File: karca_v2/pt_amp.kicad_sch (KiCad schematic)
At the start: 12 parts, among them J6 Screw_Terminal_01x10, U10 TLV9304xD, U12 NUP4202, U34 MCP3204, U9 TLV9304xD

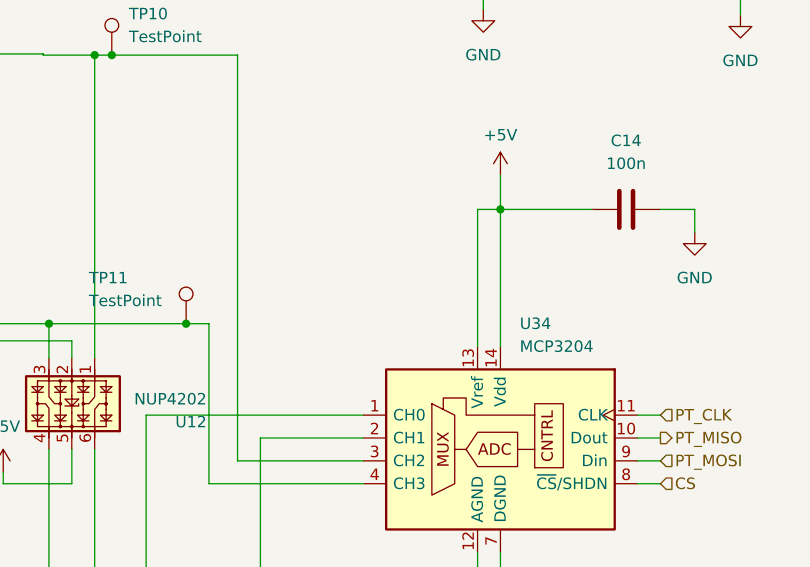
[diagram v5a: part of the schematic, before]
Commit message: finished schematic for v2.1
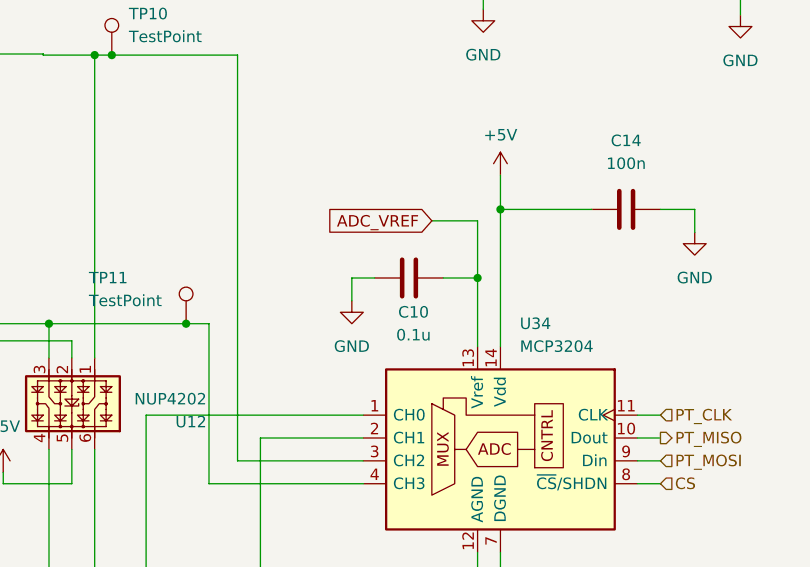
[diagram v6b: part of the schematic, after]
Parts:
- added C10: 0.1u, Capacitor_SMD:C_1206_3216Metric, symbol Device:C
- U34: footprint (none) -> Package_SO:SOIC-14_3.9x8.7mm_P1.27mm
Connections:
- net +5V: no longer U34.13 (Vref)
- net GND: now also C10.1
- new net ADC_VREF: C10.2, U34.13 (Vref)
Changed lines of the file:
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@@
+	)
+	(junction
+		(at 209.55 86.36)
+		(diameter 0)
+		(color 0 0 0 0)
 	)
 	(junction
@@
 	(wire
 		(pts
-			(xy 209.55 78.74) (xy 209.55 93.98)
-		)
-		(stroke
-			(width 0)
-			(type default)
-		)
-	)
-	(wire
-		(pts
 			(xy 64.77 94.615) (xy 64.77 99.695)
 		)
@@
 	(wire
 		(pts
+			(xy 209.55 86.36) (xy 205.74 86.36)
+		)
+		(stroke
+			(width 0)
+			(type default)
+		)
+	)
+	(wire
+		(pts
 			(xy 196.85 104.14) (xy 185.42 104.14)
 		)
@@
 	(wire
 		(pts
+			(xy 209.55 80.01) (xy 209.55 86.36)
+		)
+		(stroke
+			(width 0)
+			(type default)
+		)
+	)
+	(wire
+		(pts
 			(xy 182.88 106.68) (xy 196.85 106.68)
 		)
@@
 	(wire
 		(pts
+			(xy 195.58 88.9) (xy 195.58 86.36)
+		)
+		(stroke
+			(width 0)
+			(type default)
+		)
+	)
+	(wire
+		(pts
 			(xy 238.76 31.115) (xy 248.92 31.115)
 		)
@@
 	(wire
 		(pts
+			(xy 195.58 86.36) (xy 198.12 86.36)
+		)
+		(stroke
+			(width 0)
+			(type default)
+		)
+	)
+	(wire
+		(pts
 			(xy 227.33 101.6) (xy 229.87 101.6)
 		)
@@
 	(wire
 		(pts
+			(xy 209.55 86.36) (xy 209.55 93.98)
+		)
+		(stroke
+			(width 0)
+			(type default)
+		)
+	)
+	(wire
+		(pts
 			(xy 172.72 101.6) (xy 172.72 127)
 		)
@@
 	(wire
 		(pts
-			(xy 209.55 78.74) (xy 212.09 78.74)
+			(xy 204.47 80.01) (xy 209.55 80.01)
 		)
 		(stroke
@@
 			(width 0)
 			(type default)
+		)
+	)
+	(global_label "ADC_VREF"
+		(shape input)
+		(at 204.47 80.01 180)
+		(fields_autoplaced yes)
+		(effects
+			(font
+				(size 1.27 1.27)
+			)
+			(justify right)
+		)
+		(property "Intersheetrefs" "${INTERSHEET_REFS}"
+			(at 192.2924 80.01 0)
+			(effects
+				(font
+					(size 1.27 1.27)
+				)
+				(justify right)
+				(hide yes)
+			)
 		)
 	)
@@
 	)
 	(symbol
+		(lib_id "Device:C")
+		(at 201.93 86.36 90)
+		(unit 1)
+		(exclude_from_sim no)
+		(in_bom yes)
+		(on_board yes)
+		(dnp no)
+		(property "Reference" "C10"
+			(at 202.438 90.17 90)
+			(effects
+				(font
+					(size 1.27 1.27)
+				)
+			)
+		)
+		(property "Value" "0.1u"
+			(at 202.438 92.71 90)
+			(effects
+				(font
+					(size 1.27 1.27)
+				)
+			)
+		)
+		(property "Footprint" "Capacitor_SMD:C_1206_3216Metric"
+			(at 205.74 85.3948 0)
+			(effects
+				(font
+					(size 1.27 1.27)
+				)
+				(hide yes)
+			)
+		)
+		(property "Datasheet" "~"
+			(at 201.93 86.36 0)
+			(effects
+				(font
+					(size 1.27 1.27)
+				)
+				(hide yes)
+			)
+		)
+		(property "Description" ""
+			(at 201.93 86.36 0)
+			(effects
+				(font
+					(size 1.27 1.27)
+				)
+				(hide yes)
+			)
+		)
+		(pin "2"
+		)
+		(pin "1"
+		)
+		(instances
+			(project "karca_v2"
+				(path "/29cf4797-56f2-4f57-ae95-7df639362e3c/c566ee8f-cb19-4e44-a9af-dd67a0aa158e"
+					(reference "C10")
+					(unit 1)
+				)
+			)
+		)
+	)
+	(symbol
 		(lib_id "Connector:Screw_Terminal_01x10")
 		(at 44.45 94.615 0)
@@
 			)
 		)
-		(property "Footprint" ""
+		(property "Footprint" "Package_SO:SOIC-14_3.9x8.7mm_P1.27mm"
 			(at 234.95 111.76 0)
 			(effects
@@
 					(unit 1)
 				)
+			)
+		)
+	)
+	(symbol
+		(lib_id "power:GND")
+		(at 195.58 88.9 0)
+		(unit 1)
+		(exclude_from_sim no)
+		(in_bom yes)
+		(on_board yes)
+		(dnp no)
+		(fields_autoplaced yes)
+		(property "Reference" "#PWR043"
+			(at 195.58 95.25 0)
+			(effects
+				(font
+					(size 1.27 1.27)
+				)
+				(hide yes)
+			)
+		)
+		(property "Value" "GND"
+			(at 195.58 93.98 0)
+			(effects
+				(font
+					(size 1.27 1.27)
+				)
+			)
+		)
+		(property "Footprint" ""
+			(at 195.58 88.9 0)
+			(effects
+				(font
+					(size 1.27 1.27)
+				)
+				(hide yes)
+			)
+		)
+		(property "Datasheet" ""
+			(at 195.58 88.9 0)
+			(effects
+				(font
+					(size 1.27 1.27)
+				)
+				(hide yes)
+			)
+		)
+		(property "Description" ""
+			(at 195.58 88.9 0)
+			(effects
+				(font
+					(size 1.27 1.27)
+				)
+				(hide yes)
+			)
+		)
+		(pin "1"
+		)
+		(instances
+			(project "karca_v2"
+				(path "/29cf4797-56f2-4f57-ae95-7df639362e3c/c566ee8f-cb19-4e44-a9af-dd67a0aa158e"
+					(reference "#PWR043")
+					(unit 1)
+				)

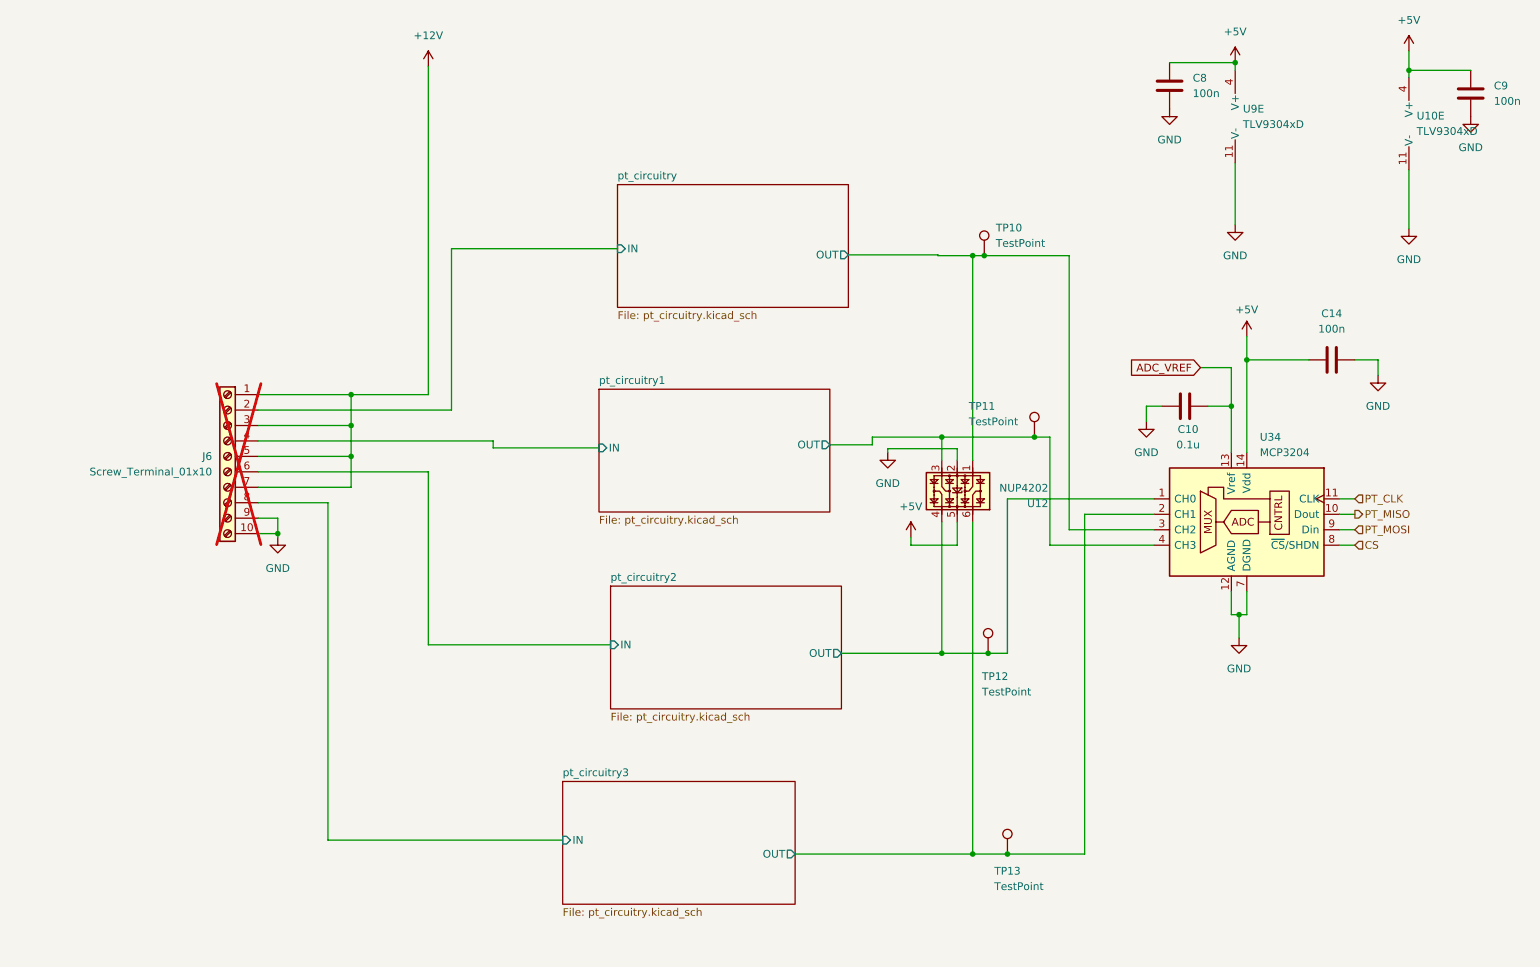
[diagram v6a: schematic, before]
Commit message: swapped adcs
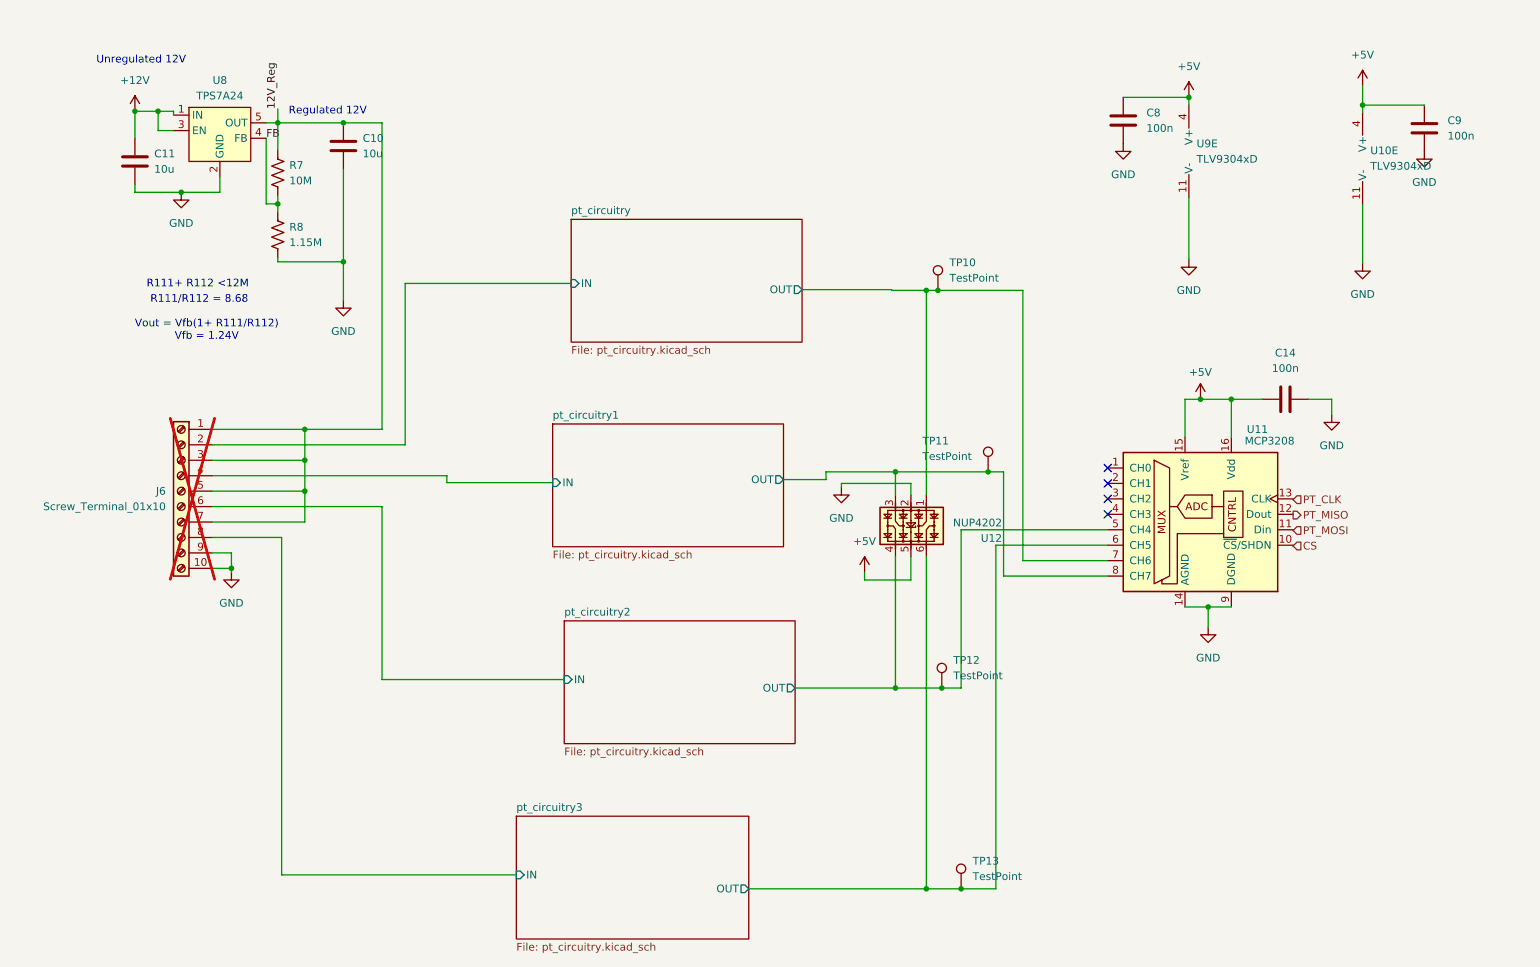
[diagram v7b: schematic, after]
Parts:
- removed U34: MCP3204, Package_SO:SOIC-14_3.9x8.7mm_P1.27mm, symbol Analog_ADC:MCP3204
- added C11: 10u, Capacitor_SMD:C_1206_3216Metric, symbol Device:C
- added R7: 10M, Resistor_SMD:R_1206_3216Metric, symbol Device:R_US
- added R8: 1.15M, Resistor_SMD:R_1206_3216Metric, symbol Device:R_US
- added U11: MCP3208, Package_SO:SOIC-16_3.9x9.9mm_P1.27mm, symbol Analog_ADC:MCP3208
- added U8: TPS7A24, Package_TO_SOT_SMD:SOT-23-5, symbol karca_lib:TPS7A24
- C10: value 0.1u -> 10u
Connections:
- net ADC_VREF is gone; now on net GND: C10.2
- net +12V: now also C11.1, U8.1 (IN), U8.3 (EN); no longer J6.1 (Pin_1), J6.3 (Pin_3), J6.5 (Pin_5), J6.7 (Pin_7)
- net +5V: now also U11.15 (Vref), U11.16 (Vdd)
- net CS: now also U11.10 (~{CS}/SHDN)
- net GND: now also C11.2, R8.2, U11.14 (AGND), U11.9 (DGND), U8.2 (GND); no longer C10.1
- net PT_CLK: now also U11.13 (CLK)
- net PT_MISO: now also U11.12 (Dout)
- net PT_MOSI: now also U11.11 (Din)
- net pt_circuitry/OUT: now also U11.7 (CH6)
- net pt_circuitry1/OUT: now also U11.8 (CH7)
- net pt_circuitry2/OUT: now also U11.5 (CH4)
- net pt_circuitry3/OUT: now also U11.6 (CH5)
- new net 12V_Reg: C10.1, J6.1 (Pin_1), J6.3 (Pin_3), J6.5 (Pin_5), J6.7 (Pin_7), R7.1, U8.5 (OUT)
- new net FB: R7.2, R8.1, U8.4 (FB)
- no-connect marks 0 -> 4
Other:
- note added: "R111+ R112 <12M"
- note added: "R111/R112 = 8.68"
- note added: "Regulated 12V"
- note added: "Unregulated 12V"
- note added: "Vout = Vfb(1+ R111/R112) Vfb = 1.24V"
- moved on the sheet: C14, C8, C9, J6, TP10, TP11, TP12, TP13, U10E, U12, U9E

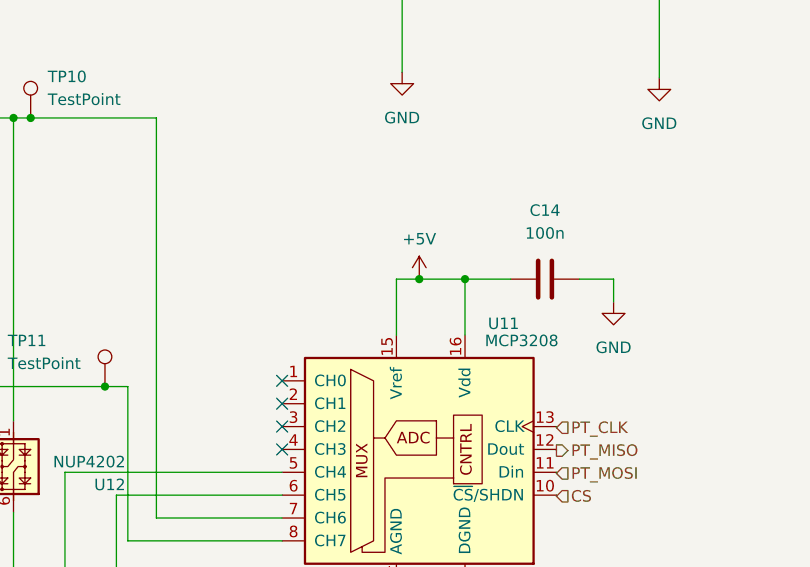
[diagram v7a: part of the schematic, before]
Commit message: added precision shunt reference to ADCs and second SPI bus for driver current and battery voltage monitors
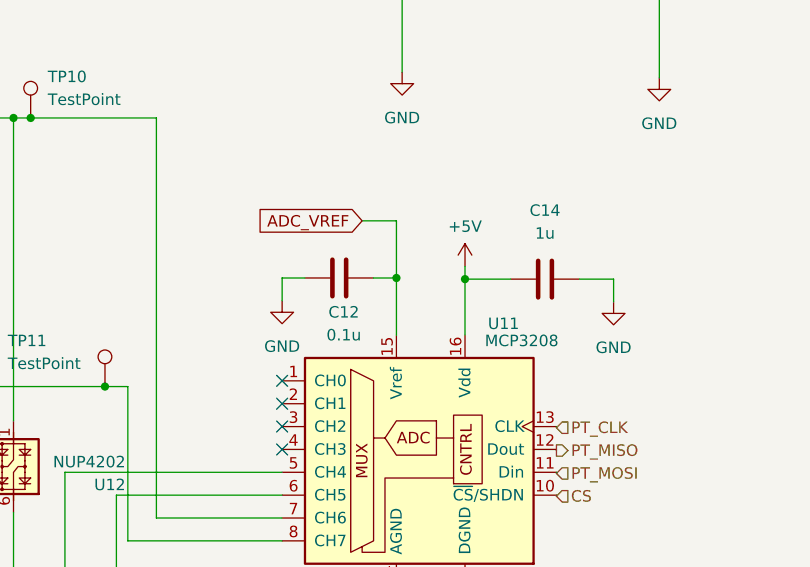
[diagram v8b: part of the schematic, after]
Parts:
- added C12: 0.1u, Capacitor_SMD:C_0805_2012Metric, symbol Device:C
- C14: value 100n -> 1u; footprint Capacitor_SMD:C_1206_3216Metric -> Capacitor_SMD:C_0805_2012Metric
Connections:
- net +5V: no longer U11.15 (Vref)
- net GND: now also C12.1
- new net ADC_VREF: C12.2, U11.15 (Vref)
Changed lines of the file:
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@@
+	)
+	(junction
+		(at 201.93 85.09)
+		(diameter 0)
+		(color 0 0 0 0)
 	)
 	(junction
@@
 	)
 	(junction
-		(at 204.47 85.217)
-		(diameter 0)
-		(color 0 0 0 0)
-	)
-	(junction
 		(at 33.02 37.846)
 		(diameter 0)
@@
 	(wire
 		(pts
+			(xy 198.12 78.74) (xy 201.93 78.74)
+		)
+		(stroke
+			(width 0)
+			(type default)
+		)
+	)
+	(wire
+		(pts
 			(xy 29.21 37.846) (xy 33.02 37.846)
 		)
@@
 	(wire
 		(pts
+			(xy 189.23 85.09) (xy 191.77 85.09)
+		)
+		(stroke
+			(width 0)
+			(type default)
+		)
+	)
+	(wire
+		(pts
 			(xy 159.385 67.31) (xy 161.29 67.31)
 		)
@@
 	(wire
 		(pts
+			(xy 201.93 78.74) (xy 201.93 85.09)
+		)
+		(stroke
+			(width 0)
+			(type default)
+		)
+	)
+	(wire
+		(pts
 			(xy 57.15 90.17) (xy 57.15 95.25)
 		)
@@
 	(wire
 		(pts
+			(xy 209.55 85.217) (xy 209.55 91.44)
+		)
+		(stroke
+			(width 0)
+			(type default)
+		)
+	)
+	(wire
+		(pts
 			(xy 57.15 100.33) (xy 57.15 105.41)
 		)
@@
 	(wire
 		(pts
+			(xy 199.39 85.09) (xy 201.93 85.09)
+		)
+		(stroke
+			(width 0)
+			(type default)
+		)
+	)
+	(wire
+		(pts
 			(xy 73.66 92.71) (xy 73.66 66.167)
 		)
@@
 	(wire
 		(pts
+			(xy 189.23 87.63) (xy 189.23 85.09)
+		)
+		(stroke
+			(width 0)
+			(type default)
+		)
+	)
+	(wire
+		(pts
 			(xy 175.26 111.76) (xy 189.23 111.76)
 		)
@@
 	(wire
 		(pts
+			(xy 209.55 83.82) (xy 209.55 85.217)
+		)
+		(stroke
+			(width 0)
+			(type default)
+		)
+	)
+	(wire
+		(pts
 			(xy 69.85 39.751) (xy 69.85 90.17)
 		)
@@
 	(wire
 		(pts
-			(xy 209.55 91.44) (xy 209.55 85.217)
-		)
-		(stroke
-			(width 0)
-			(type default)
-		)
-	)
-	(wire
-		(pts
 			(xy 29.21 37.846) (xy 29.21 42.291)
 		)
@@
 	(wire
 		(pts
+			(xy 201.93 91.44) (xy 201.93 85.09)
+		)
+		(stroke
+			(width 0)
+			(type default)
+		)
+	)
+	(wire
+		(pts
 			(xy 69.85 131.318) (xy 69.85 102.87)
 		)
@@
 	(wire
 		(pts
-			(xy 201.93 91.44) (xy 201.93 85.217)
-		)
-		(stroke
-			(width 0)
-			(type default)
-		)
-	)
-	(wire
-		(pts
 			(xy 35.56 37.846) (xy 35.56 38.481)
 		)
@@
 	(wire
 		(pts
-			(xy 201.93 85.217) (xy 204.47 85.217)
-		)
-		(stroke
-			(width 0)
-			(type default)
-		)
-	)
-	(wire
-		(pts
 			(xy 53.34 163.449) (xy 91.948 163.449)
 		)
@@
 		(pts
 			(xy 154.305 97.155) (xy 169.545 97.155)
-		)
-		(stroke
-			(width 0)
-			(type default)
-		)
-	)
-	(wire
-		(pts
-			(xy 209.55 85.217) (xy 204.47 85.217)
 		)
 		(stroke
@@
 			)
 			(justify left bottom)
+		)
+	)
+	(global_label "ADC_VREF"
+		(shape input)
+		(at 198.12 78.74 180)
+		(fields_autoplaced yes)
+		(effects
+			(font
+				(size 1.27 1.27)
+			)
+			(justify right)
+		)
+		(property "Intersheetrefs" "${INTERSHEET_REFS}"
+			(at 185.9424 78.74 0)
+			(effects
+				(font
+					(size 1.27 1.27)
+				)
+				(justify right)
+				(hide yes)
+			)
 		)
 	)
@@
 			)
 		)
-		(property "Value" "100n"
+		(property "Value" "1u"
 			(at 218.44 80.137 90)
 			(effects
@@
 			)
 		)
-		(property "Footprint" "Capacitor_SMD:C_1206_3216Metric"
+		(property "Footprint" "Capacitor_SMD:C_0805_2012Metric"
 			(at 222.25 84.2518 0)
 			(effects
@@
 	)
 	(symbol
+		(lib_id "Device:C")
+		(at 195.58 85.09 90)
+		(unit 1)
+		(exclude_from_sim no)
+		(in_bom yes)
+		(on_board yes)
+		(dnp no)
+		(property "Reference" "C12"
+			(at 196.088 88.9 90)
+			(effects
+				(font
+					(size 1.27 1.27)
+				)
+			)
+		)
+		(property "Value" "0.1u"
+			(at 196.088 91.44 90)
+			(effects
+				(font
+					(size 1.27 1.27)
+				)
+			)
+		)
+		(property "Footprint" "Capacitor_SMD:C_0805_2012Metric"
+			(at 199.39 84.1248 0)
+			(effects
+				(font
+					(size 1.27 1.27)
+				)
+				(hide yes)
+			)
+		)
+		(property "Datasheet" "~"
+			(at 195.58 85.09 0)
+			(effects
+				(font
+					(size 1.27 1.27)
+				)
+				(hide yes)
+			)
+		)
+		(property "Description" ""
+			(at 195.58 85.09 0)
+			(effects
+				(font
+					(size 1.27 1.27)
+				)
+				(hide yes)
+			)
+		)
+		(pin "2"
+		)
+		(pin "1"
+		)
+		(instances
+			(project "karca_v2"
+				(path "/29cf4797-56f2-4f57-ae95-7df639362e3c/c566ee8f-cb19-4e44-a9af-dd67a0aa158e"
+					(reference "C12")
+					(unit 1)
+				)
+			)
+		)
+	)
+	(symbol
 		(lib_id "power:GND")
 		(at 45.085 113.665 0)
@@
 	(symbol
 		(lib_id "power:GND")
+		(at 189.23 87.63 0)
+		(unit 1)
+		(exclude_from_sim no)
+		(in_bom yes)
+		(on_board yes)
+		(dnp no)
+		(fields_autoplaced yes)
+		(property "Reference" "#PWR052"
+			(at 189.23 93.98 0)
+			(effects
+				(font
+					(size 1.27 1.27)
+				)
+				(hide yes)
+			)
+		)
+		(property "Value" "GND"
+			(at 189.23 92.71 0)
+			(effects
+				(font
+					(size 1.27 1.27)
+				)
+			)
+		)
+		(property "Footprint" ""
+			(at 189.23 87.63 0)
+			(effects
+				(font
+					(size 1.27 1.27)
+				)
+				(hide yes)
+			)
+		)
+		(property "Datasheet" ""
+			(at 189.23 87.63 0)
+			(effects
+				(font
+					(size 1.27 1.27)
+				)
+				(hide yes)
+			)
+		)
+		(property "Description" ""
+			(at 189.23 87.63 0)
+			(effects
+				(font
+					(size 1.27 1.27)
+				)
+				(hide yes)
+			)
+		)
+		(pin "1"
+		)
+		(instances
+			(project "karca_v2"
+				(path "/29cf4797-56f2-4f57-ae95-7df639362e3c/c566ee8f-cb19-4e44-a9af-dd67a0aa158e"
+					(reference "#PWR052")
+					(unit 1)
+				)
+			)
+		)
+	)
+	(symbol
+		(lib_id "power:GND")
 		(at 231.14 62.865 0)
 		(unit 1)
@@
 	(symbol
 		(lib_id "power:+5V")
-		(at 204.47 85.217 0)
+		(at 209.55 83.82 0)
 		(unit 1)
 		(exclude_from_sim no)
@@
 		(fields_autoplaced yes)
 		(property "Reference" "#PWR044"
-			(at 204.47 89.027 0)
+			(at 209.55 87.63 0)
 			(effects
 				(font
@@
 		)
 		(property "Value" "+5V"
-			(at 204.47 80.772 0)
+			(at 209.55 79.375 0)
 			(effects
 				(font
@@
 		)
 		(property "Footprint" ""
-			(at 204.47 85.217 0)
+			(at 209.55 83.82 0)
 			(effects
 				(font
@@
 		)
 		(property "Datasheet" ""
-			(at 204.47 85.217 0)
+			(at 209.55 83.82 0)
 			(effects
 				(font
@@
 		)
 		(property "Description" ""
-			(at 204.47 85.217 0)
-			(effects
-				(font
+			(at 209.55 83.82 0)
+			(effects
+				(font
